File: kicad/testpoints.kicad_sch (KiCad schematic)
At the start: 1 part

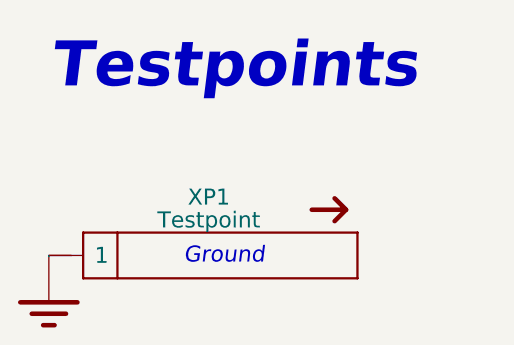
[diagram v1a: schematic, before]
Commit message: Add voltage value to caps, update BOM, SCH, ASM
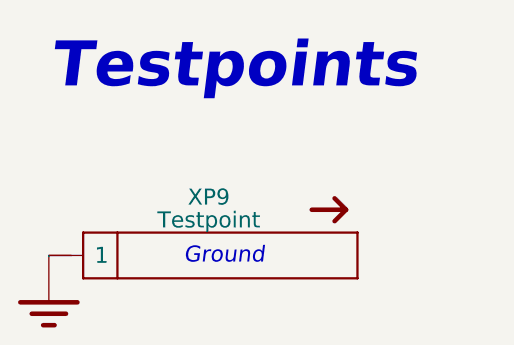
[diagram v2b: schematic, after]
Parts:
- XP9: renamed from XP1; now left out of the parts list
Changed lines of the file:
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@@
   )
   (symbol (lib_id "Connectors:XP_PIN_ARR1") (at 157.48 104.775 0) (unit 1)
-    (in_bom yes) (on_board yes)
-    (property "Reference" "XP1" (id 0) (at 157.48 95.758 0)
+    (in_bom no) (on_board yes)
+    (property "Reference" "XP9" (id 0) (at 157.48 95.758 0)
       (effects (font (size 1.778 1.778)))
     )

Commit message: Add wiring diagram; Add work ours (stage 2); refactor folders
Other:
- title: (none) -> RadioSens v1
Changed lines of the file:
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@@
 (kicad_sch (version 20211123) (generator eeschema)
   (paper "A4")
+  (title_block
+    (title "RadioSens v1")
+    (comment 2 "Electrical Circuit")
+  )
   (wire (pts (xy 139.7 102.362) (xy 139.7 102.235))
     (stroke (width 0) (type default) (color 0 0 0 0))
